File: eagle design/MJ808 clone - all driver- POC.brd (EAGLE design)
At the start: 35 x 35 mm, 28 parts, among them IC1 ATTINY4313-MMH, IC2 PRQV8.00CR1510Y00L, IC3 MCP2515, IC5 MCP2561-2, IC6 MAX16820, IC7 LDK320ADU50R, K1 CRTL, Q1 SiA456DJ, X3 BAT

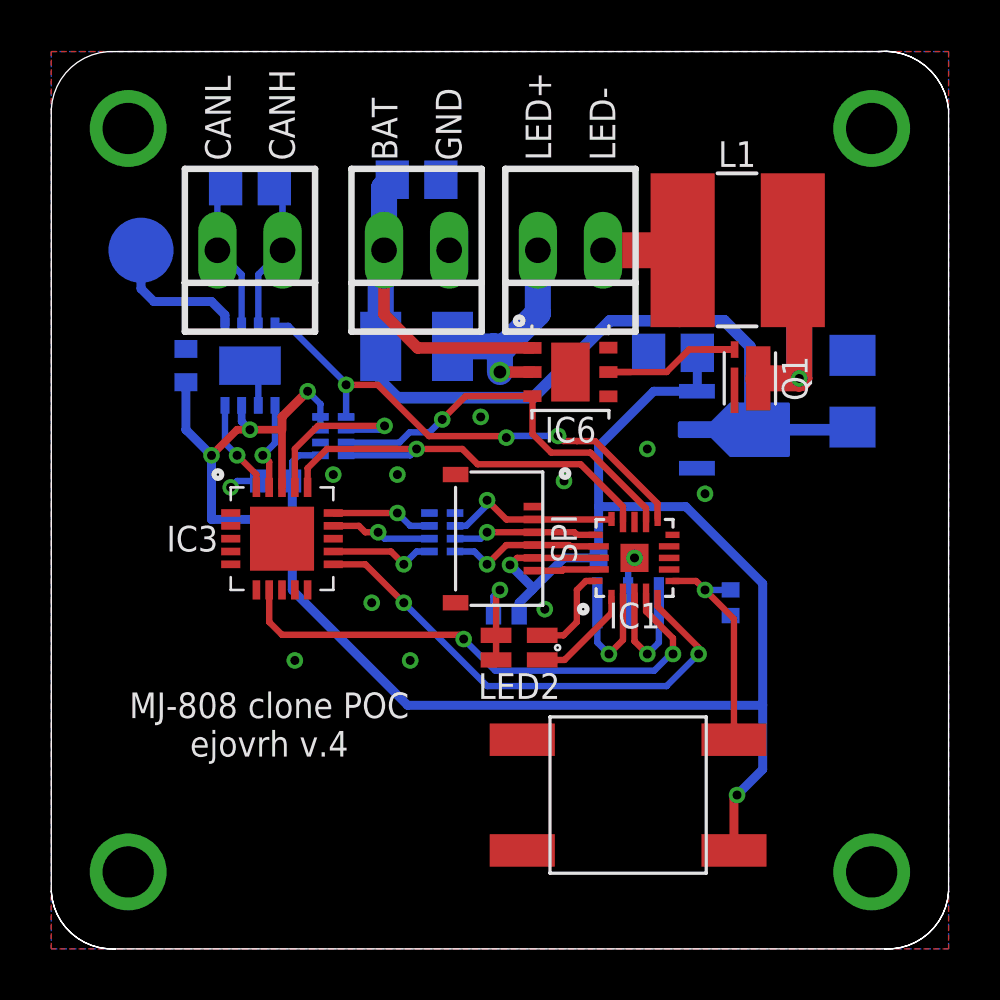
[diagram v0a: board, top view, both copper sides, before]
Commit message: - synced POC board with production board - corrected name and value placements on both boards - work on production board still continues
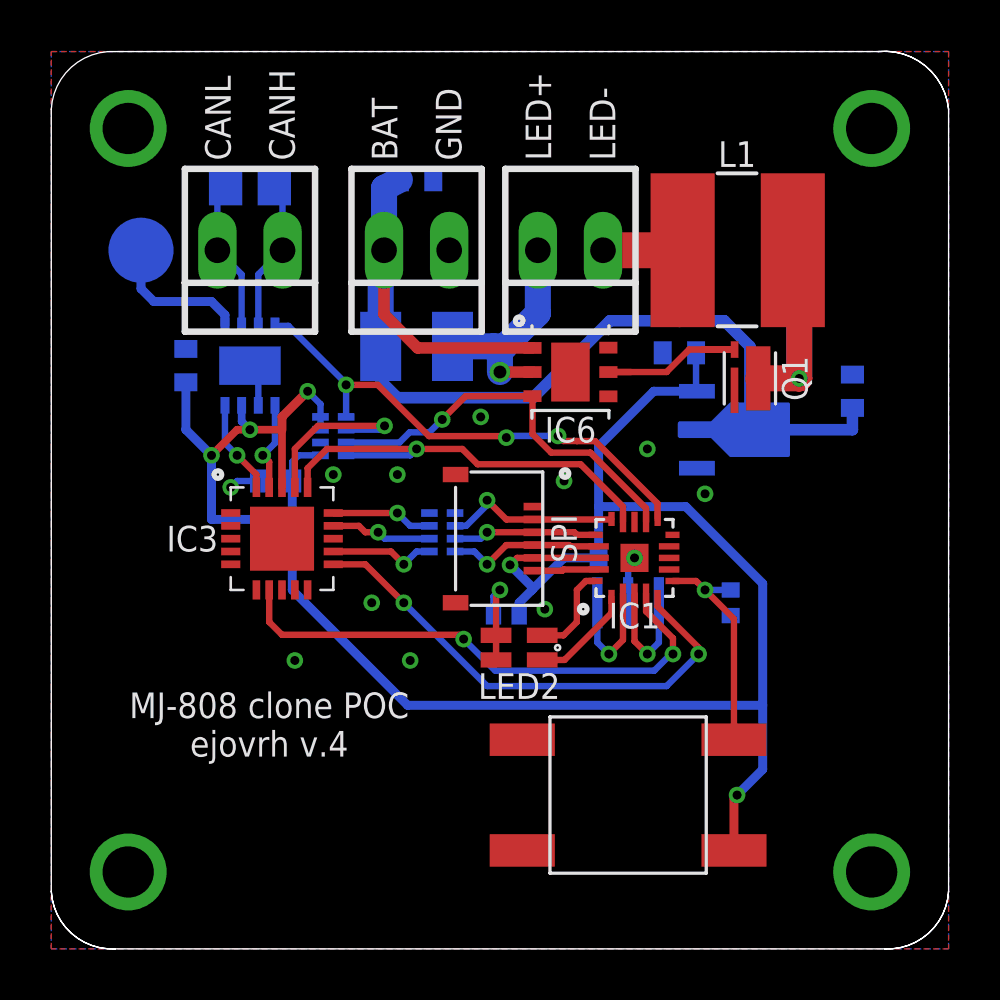
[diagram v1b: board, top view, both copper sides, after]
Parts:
- C3: value 100μF -> 1μF / 10V; device rcl:C1206 -> rcl:C0402
- C4: value 47μF -> 1μF; device rcl:C0805 -> rcl:C0402
- C6: device rcl:C0805 -> rcl:C0402
- moved C4 0.25 mm to (24.5, 23.2)
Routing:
- net BAT+: track 47.3 -> 48.4 mm
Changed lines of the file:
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@@
 <grid distance="0.25" unitdist="mm" unit="mm" style="lines" multiple="1" display="yes" altdistance="0.25" altunitdist="mm" altunit="mm"/>
 <layers>
-<layer number="1" name="Top" color="4" fill="1" visible="yes" active="yes"/>
+<layer number="1" name="Top" color="4" fill="1" visible="no" active="yes"/>
 <layer number="2" name="Route2" color="1" fill="3" visible="no" active="no"/>
 <layer number="3" name="Route3" color="4" fill="3" visible="no" active="no"/>
@@
 <layer number="14" name="Route14" color="1" fill="6" visible="no" active="no"/>
 <layer number="15" name="Route15" color="4" fill="6" visible="no" active="no"/>
-<layer number="16" name="Bottom" color="1" fill="1" visible="no" active="yes"/>
+<layer number="16" name="Bottom" color="1" fill="1" visible="yes" active="yes"/>
 <layer number="17" name="Pads" color="2" fill="1" visible="yes" active="yes"/>
 <layer number="18" name="Vias" color="2" fill="1" visible="yes" active="yes"/>
 <layer number="19" name="Unrouted" color="6" fill="1" visible="yes" active="yes"/>
 <layer number="20" name="Dimension" color="24" fill="1" visible="yes" active="yes"/>
-<layer number="21" name="tPlace" color="7" fill="1" visible="yes" active="yes"/>
-<layer number="22" name="bPlace" color="7" fill="1" visible="no" active="yes"/>
-<layer number="23" name="tOrigins" color="15" fill="1" visible="yes" active="yes"/>
-<layer number="24" name="bOrigins" color="15" fill="1" visible="no" active="yes"/>
-<layer number="25" name="tNames" color="7" fill="1" visible="yes" active="yes"/>
-<layer number="26" name="bNames" color="7" fill="1" visible="no" active="yes"/>
+<layer number="21" name="tPlace" color="7" fill="1" visible="no" active="yes"/>
+<layer number="22" name="bPlace" color="7" fill="1" visible="yes" active="yes"/>
+<layer number="23" name="tOrigins" color="15" fill="1" visible="no" active="yes"/>
+<layer number="24" name="bOrigins" color="15" fill="1" visible="yes" active="yes"/>
+<layer number="25" name="tNames" color="7" fill="1" visible="no" active="yes"/>
+<layer number="26" name="bNames" color="7" fill="1" visible="yes" active="yes"/>
 <layer number="27" name="tValues" color="7" fill="1" visible="no" active="yes"/>
 <layer number="28" name="bValues" color="7" fill="1" visible="no" active="yes"/>
@@
 <layer number="37" name="tTest" color="7" fill="1" visible="no" active="yes"/>
 <layer number="38" name="bTest" color="7" fill="1" visible="no" active="yes"/>
-<layer number="39" name="tKeepout" color="4" fill="11" visible="yes" active="yes"/>
-<layer number="40" name="bKeepout" color="1" fill="11" visible="no" active="yes"/>
-<layer number="41" name="tRestrict" color="4" fill="10" visible="yes" active="yes"/>
-<layer number="42" name="bRestrict" color="1" fill="10" visible="no" active="yes"/>
+<layer number="39" name="tKeepout" color="4" fill="11" visible="no" active="yes"/>
+<layer number="40" name="bKeepout" color="1" fill="11" visible="yes" active="yes"/>
+<layer number="41" name="tRestrict" color="4" fill="10" visible="no" active="yes"/>
+<layer number="42" name="bRestrict" color="1" fill="10" visible="yes" active="yes"/>
 <layer number="43" name="vRestrict" color="2" fill="10" visible="yes" active="yes"/>
 <layer number="44" name="Drills" color="7" fill="1" visible="no" active="yes"/>
@@
 <layer number="49" name="Reference" color="7" fill="1" visible="no" active="yes"/>
 <layer number="50" name="dxf" color="7" fill="1" visible="no" active="no"/>
-<layer number="51" name="tDocu" color="7" fill="1" visible="yes" active="yes"/>
-<layer number="52" name="bDocu" color="7" fill="1" visible="no" active="yes"/>
+<layer number="51" name="tDocu" color="7" fill="1" visible="no" active="yes"/>
+<layer number="52" name="bDocu" color="7" fill="1" visible="yes" active="yes"/>
 <layer number="53" name="tGND_GNDA" color="7" fill="9" visible="no" active="no"/>
 <layer number="54" name="bGND_GNDA" color="1" fill="9" visible="no" active="no"/>
@@
 </autorouter>
 <elements>
-<element name="C6" library="rcl" library_urn="urn:adsk.eagle:library:334" package="C0805" package3d_urn="urn:adsk.eagle:package:23617/2" value="1μF / 10V" x="14.25" y="30" smashed="yes" rot="MR180">
+<element name="C6" library="rcl" library_urn="urn:adsk.eagle:library:334" package="C0402" package3d_urn="urn:adsk.eagle:package:23626/1" value="1μF / 10V" x="14.25" y="30" smashed="yes" rot="MR180">
 <attribute name="NAME" x="14.25" y="31.75" size="1" layer="26" font="vector" rot="MR180" align="center"/>
 <attribute name="SPICEPREFIX" value="C" x="14.25" y="30" size="1.778" layer="28" rot="MR180" display="off"/>
@@
 </element>
 <element name="C2" library="rcl" library_urn="urn:adsk.eagle:library:334" package="C0402" package3d_urn="urn:adsk.eagle:package:23626/1" value="0.1μF" x="8.75" y="18.25" smashed="yes" rot="MR0">
-<attribute name="NAME" x="5.5" y="18.25" size="1" layer="26" font="vector" rot="MR0" align="center"/>
+<attribute name="NAME" x="8.75" y="17" size="1" layer="26" font="vector" rot="MR0" align="center"/>
 <attribute name="SPICEPREFIX" value="C" x="8.75" y="18.25" size="1.778" layer="28" rot="MR0" display="off"/>
 <attribute name="VALUE" x="9.385" y="16.345" size="1.27" layer="28" rot="MR0"/>
@@
 </element>
 <element name="R10" library="rcl" library_urn="urn:adsk.eagle:library:334" package="R1210" package3d_urn="urn:adsk.eagle:package:23554/2" value="0.15 / 1W" x="14.25" y="23.5" smashed="yes" rot="MR0">
-<attribute name="NAME" x="14.25" y="24.75" size="1" layer="26" font="vector" rot="MR0" align="center"/>
+<attribute name="NAME" x="14.25" y="25.75" size="1" layer="26" font="vector" rot="MR0" align="center"/>
 <attribute name="SPICEPREFIX" value="R" x="14.25" y="23.5" size="1.778" layer="28" rot="MR0" display="off"/>
 <attribute name="VALUE" x="14.885" y="20.96" size="1.27" layer="28" rot="MR0"/>
@@
 <attribute name="VALUE" x="22.79" y="32.33" size="1.016" layer="27" ratio="10" rot="R180"/>
 </element>
-<element name="C3" library="rcl" library_urn="urn:adsk.eagle:library:334" package="C1206" package3d_urn="urn:adsk.eagle:package:23618/2" value="100μF" x="31.25" y="21.75" smashed="yes" rot="MR90">
-<attribute name="NAME" x="33" y="21.75" size="1" layer="26" font="vector" rot="MR90" align="center"/>
+<element name="C3" library="rcl" library_urn="urn:adsk.eagle:library:334" package="C0402" package3d_urn="urn:adsk.eagle:package:23626/1" value="1μF / 10V" x="31.25" y="21.75" smashed="yes" rot="MR90">
+<attribute name="NAME" x="32.5" y="21.75" size="1" layer="26" font="vector" rot="MR90" align="center"/>
 <attribute name="SPICEPREFIX" value="C" x="37.05" y="21.75" size="1.778" layer="28" rot="MR90" display="off"/>
 <attribute name="VALUE" x="29.345" y="21.115" size="1.27" layer="28" rot="MR90"/>
 </element>
-<element name="C4" library="rcl" library_urn="urn:adsk.eagle:library:334" package="C0805" package3d_urn="urn:adsk.eagle:package:23617/2" value="47μF" x="24.25" y="23.25" smashed="yes" rot="MR180">
-<attribute name="NAME" x="24.25" y="21.5" size="1" layer="26" font="vector" rot="MR180" align="center"/>
-<attribute name="SPICEPREFIX" value="C" x="12.65" y="22.35" size="1.778" layer="28" rot="MR180" display="off"/>
-<attribute name="VALUE" x="23.615" y="25.155" size="1.27" layer="28" rot="MR180"/>
+<element name="C4" library="rcl" library_urn="urn:adsk.eagle:library:334" package="C0402" package3d_urn="urn:adsk.eagle:package:23626/1" value="1μF" x="24.5" y="23.25" smashed="yes" rot="MR180">
+<attribute name="NAME" x="24.5" y="24.5" size="1" layer="26" font="vector" rot="MR180" align="center"/>
+<attribute name="SPICEPREFIX" value="C" x="12.9" y="22.35" size="1.778" layer="28" rot="MR180" display="off"/>
+<attribute name="VALUE" x="23.865" y="25.155" size="1.27" layer="28" rot="MR180"/>
 </element>
 <element name="R2" library="rcl" library_urn="urn:adsk.eagle:library:334" package="R0402" package3d_urn="urn:adsk.eagle:package:23547/2" value="10k" x="17.75" y="13" smashed="yes" rot="MR180">
@@
 <wire x1="12.85" y1="27.12" x2="12.98" y2="27.25" width="1.016" layer="16"/>
 <wire x1="12.98" y1="27.25" x2="12.98" y2="29.68" width="1.016" layer="16"/>
-<wire x1="12.98" y1="29.68" x2="13.3" y2="30" width="1.016" layer="16"/>
+<wire x1="12.98" y1="29.68" x2="13.6" y2="30" width="1.016" layer="16"/>
 <wire x1="12.85" y1="23.5" x2="12.85" y2="22.15" width="0.45" layer="16"/>
 <wire x1="12.85" y1="22.15" x2="13.5" y2="21.5" width="0.45" layer="16"/>
@@
 <contactref element="C3" pad="1"/>
 <wire x1="25.185" y1="20.25" x2="27.25" y2="20.25" width="0.45" layer="16"/>
-<wire x1="27.25" y1="20.25" x2="31.15" y2="20.25" width="0.45" layer="16"/>
-<wire x1="31.15" y1="20.25" x2="31.25" y2="20.35" width="0.45" layer="16"/>
 <wire x1="27.25" y1="23.5" x2="27.25" y2="20.25" width="0.45" layer="16"/>
 <wire x1="21.79205" y1="24.5" x2="24.5" y2="24.5" width="0.45" layer="16"/>
@@
 <wire x1="13.5" y1="21.5" x2="18.79205" y2="21.5" width="0.45" layer="16"/>
 <wire x1="18.79205" y1="21.5" x2="21.79205" y2="24.5" width="0.45" layer="16"/>
+<wire x1="27.25" y1="20.25" x2="31.25" y2="20.25" width="0.45" layer="16"/>
+<wire x1="31.25" y1="20.25" x2="31.25" y2="21.1" width="0.45" layer="16"/>
 </signal>
 <signal name="GND">
@@
 <contactref element="IC7" pad="VOUT"/>
 <contactref element="C4" pad="2"/>
-<wire x1="25.2" y1="23.25" x2="25.2" y2="21.765" width="0.35" layer="16"/>
-<wire x1="25.2" y1="21.765" x2="25.185" y2="21.75" width="0.45" layer="16"/>
 <wire x1="25.185" y1="21.75" x2="23.5" y2="21.75" width="0.35" layer="16"/>
 <wire x1="21.35" y1="19.6" x2="21.35" y2="17.25" width="0.35" layer="16"/>
@@
 <wire x1="6.25" y1="19.25" x2="6.25" y2="16.75" width="0.35" layer="16"/>
 <wire x1="21.35" y1="17.25" x2="21.35" y2="15.25" width="0.35" layer="16"/>
+<wire x1="25.185" y1="21.75" x2="25.15" y2="21.785" width="0.25" layer="16"/>
+<wire x1="25.15" y1="21.785" x2="25.15" y2="23.25" width="0.25" layer="16"/>
 </signal>
 <signal name="LED_AN" class="5">
